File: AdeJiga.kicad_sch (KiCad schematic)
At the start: 33 parts, among them J1 Screw_Terminal_01x03, J10 Conn_01x02_Pin, J11 Conn_01x02_Pin, J2 Screw_Terminal_01x02, J3 Screw_Terminal_01x03, J4 Conn_01x05_Pin, J5 Conn_01x02_Pin, J6 Conn_01x03_Pin, J7 Conn_01x02_Pin, J8 Conn_01x03_Pin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

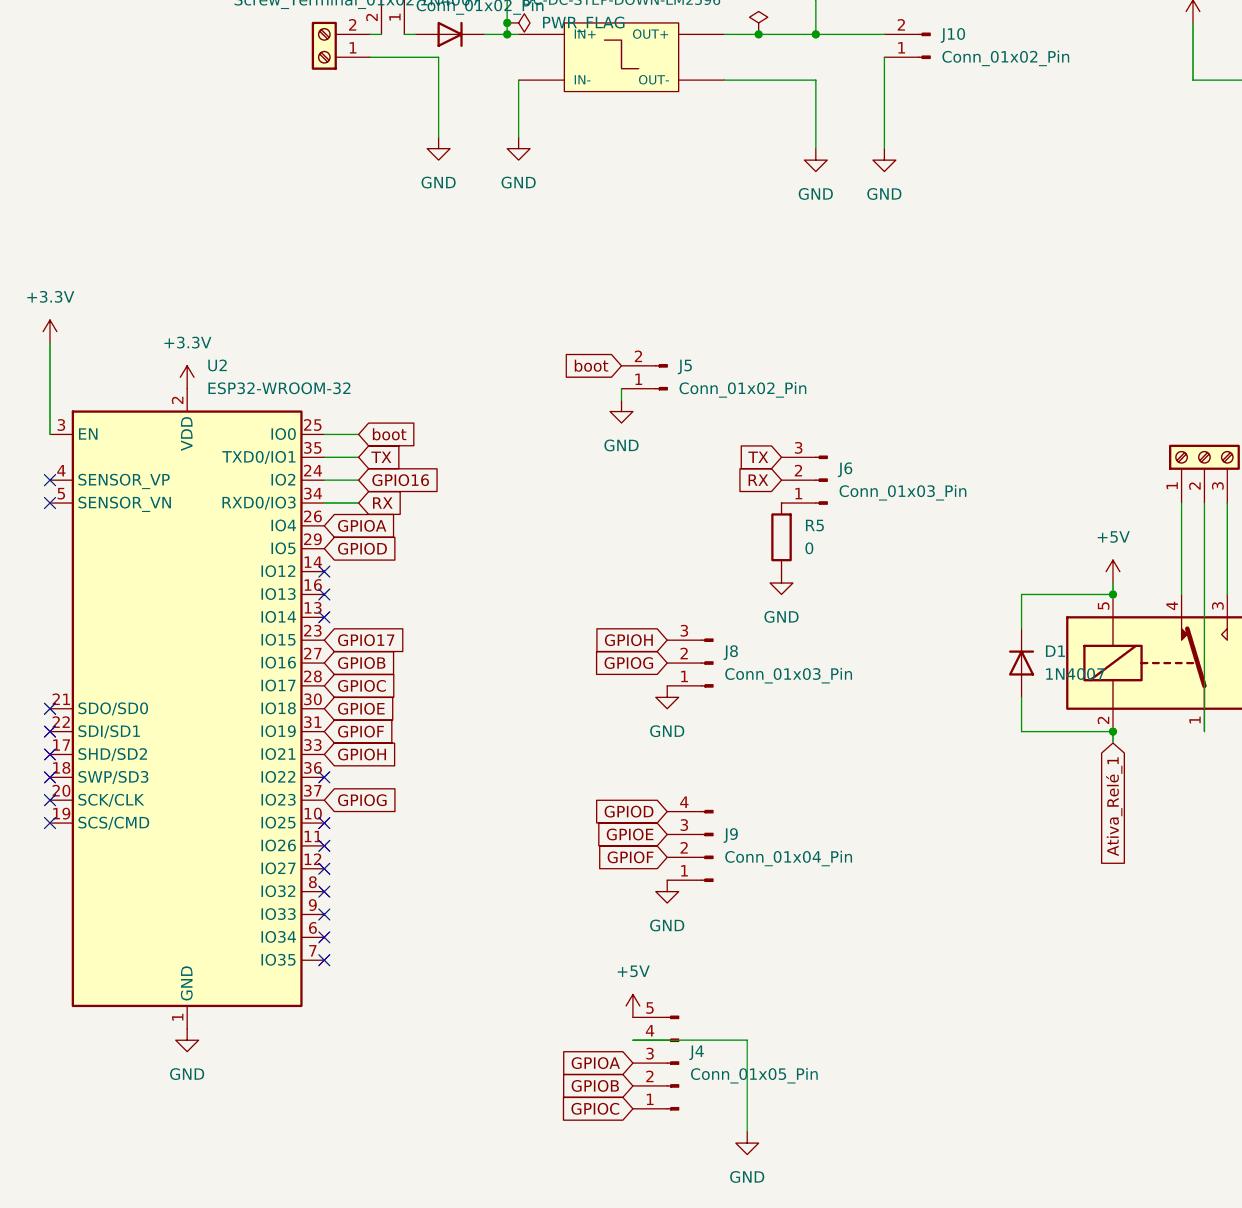
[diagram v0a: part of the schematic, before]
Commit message: Adicao dos modelos 3d e melhorias viasuais no layout
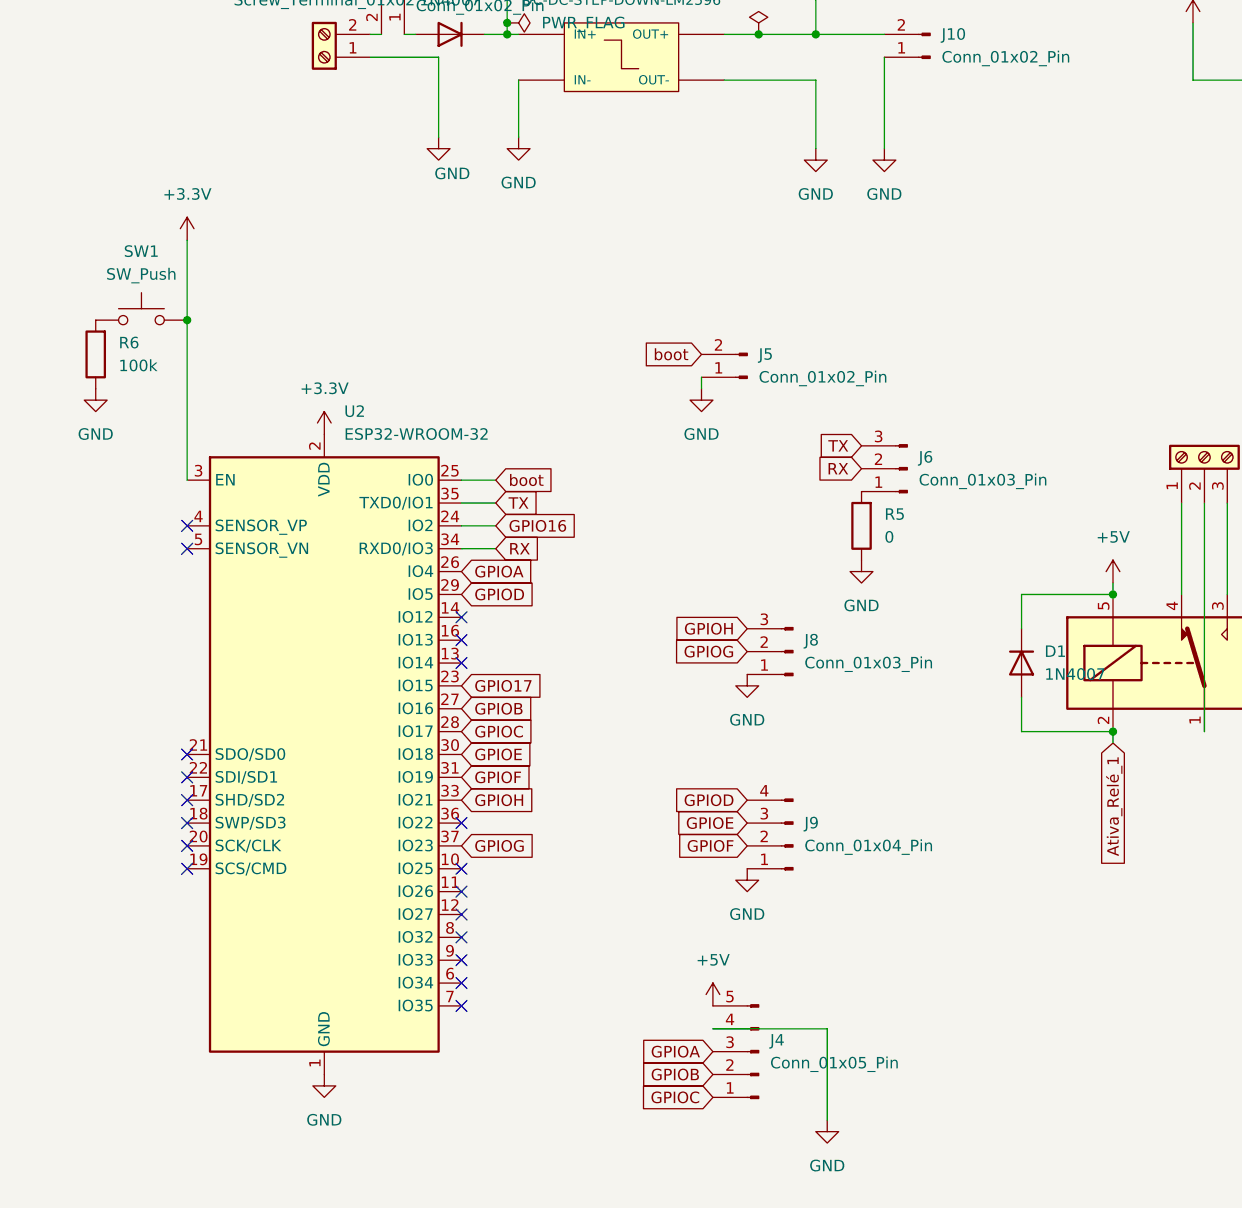
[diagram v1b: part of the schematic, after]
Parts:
- added R6: 100k, Resistor_THT:R_Axial_DIN0204_L3.6mm_D1.6mm_P5.08mm_Vertical, symbol Device:R
- added SW1: SW_Push, symbol Switch:SW_Push
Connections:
- net +3.3V: now also SW1.2
- net GND: now also R6.1
- new net: R6.2, SW1.1
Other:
- moved on the sheet: J4, J5, J6, J8, J9, R5, U2

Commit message: 3 reles na jiga
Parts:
- removed R6: 100k, Resistor_THT:R_Axial_DIN0204_L3.6mm_D1.6mm_P5.08mm_Vertical, symbol Device:R
- removed SW1: SW_Push, symbol Switch:SW_Push
- added D6: 1N4007, Diode_THT:D_DO-41_SOD81_P10.16mm_Horizontal, symbol Diode:1N4007
- added D7: LED, LED_THT:LED_D5.0mm_Clear, symbol Device:LED
- added J12: Screw_Terminal_01x03, TerminalBlock_MetzConnect:TerminalBlock_MetzConnect_Type011_RT05503HBWC_1x03_P5.00mm_Horizontal, symbol Connector:Screw_Terminal_01x03
- added K3: JJM1C_relay, Benzlab:JJM1C_relay, symbol Benzlab:JJM1C_relay
- added Q2: TIP127, Package_TO_SOT_THT:TO-220-3_Vertical, symbol Transistor_BJT:TIP127
- added R7: 220, Resistor_THT:R_Axial_DIN0207_L6.3mm_D2.5mm_P10.16mm_Horizontal, symbol Device:R
- added R8: 3.3k, Resistor_THT:R_Axial_DIN0207_L6.3mm_D2.5mm_P10.16mm_Horizontal, symbol Device:R
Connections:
- net +5V: now also D6.1 (K), K3.5
- net GND: now also D7.1 (K), Q2.3 (E)
- net REL3: now reaches U2.16 (IO13)
- net REL3: now also R7.2, R8.1
- net GPIO16 renamed REL1
- net GPIO17 renamed REL2
- new net: D7.2 (A), R7.1
- new net: Q2.1 (B), R8.2
- new net: J12.2 (Pin_2), K3.1
- new net: J12.3 (Pin_3), K3.3
- new net: J12.1 (Pin_1), K3.4
- new net Ativa_Relé_3: D6.2 (A), K3.2, Q2.2 (C)
- no-connect marks 19 -> 18
